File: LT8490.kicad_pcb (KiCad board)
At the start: 2 copper layers, 44 x 52 mm, 82 parts, among them Q1 TBD, Q2 TBD, Q3 TBD, Q4 TBD, Q5 BSS84, Q6 MBT2222ADW1T1, U4 LT8490EUKJPBF

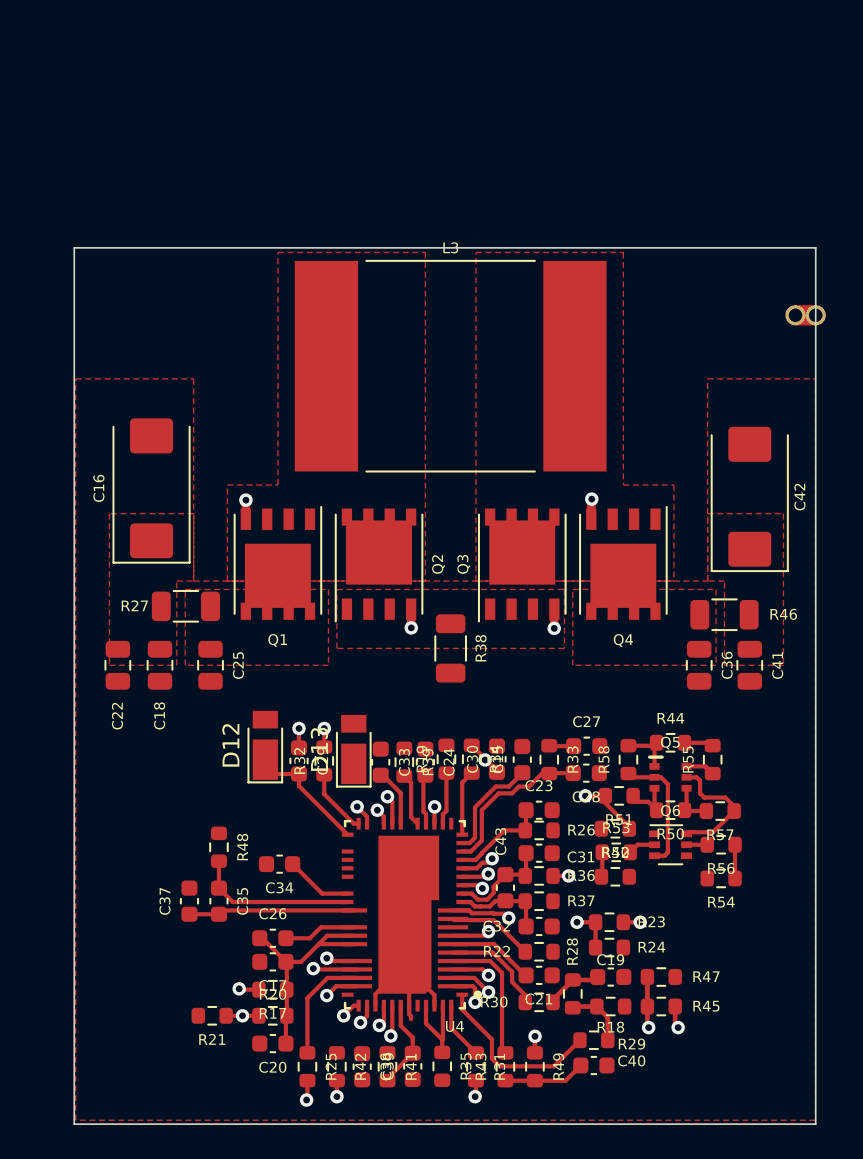
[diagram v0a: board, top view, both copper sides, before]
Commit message: routed on 6 layers. Possible to do 4?
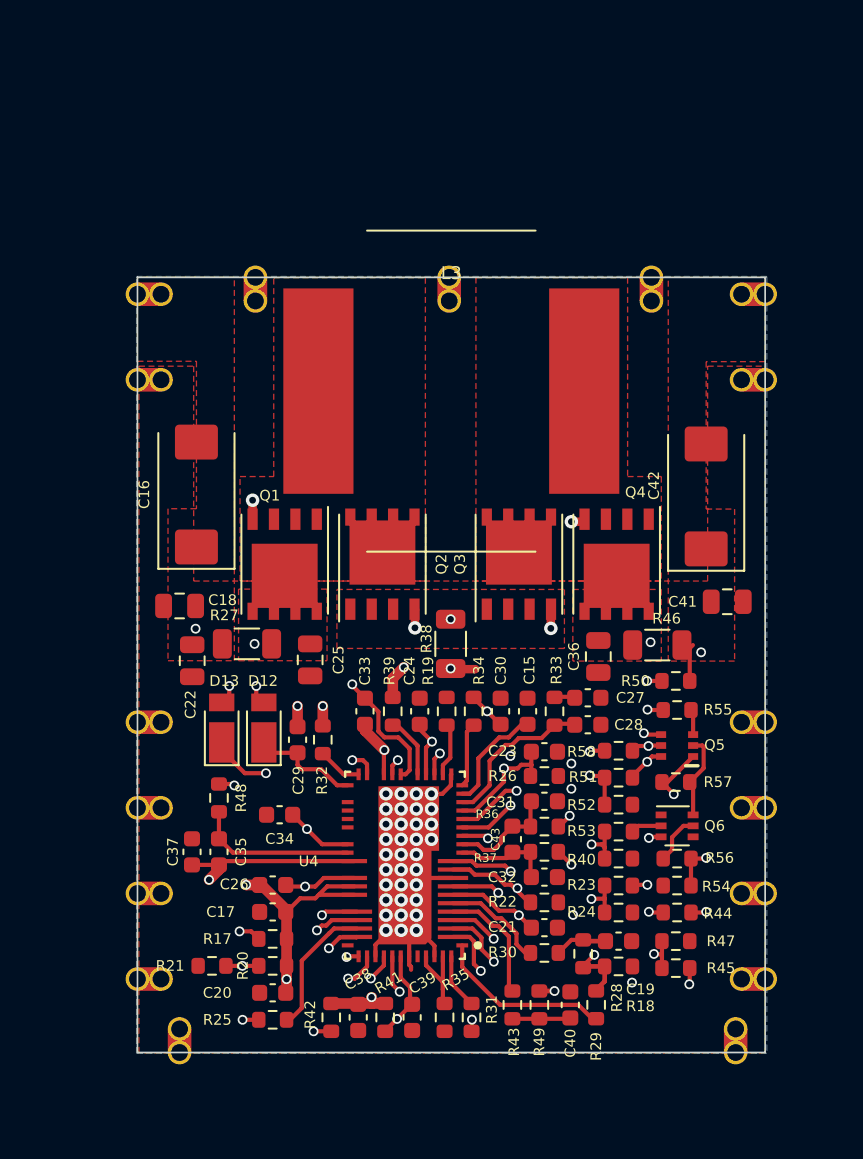
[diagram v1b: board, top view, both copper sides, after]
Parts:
- removed the REF** at (169.5, 78.0)
- added NT1: NetTie_2, NetTie:NetTie-2_SMD_Pad0.5mm, F.Cu at (148.8, 99.0)
- added REF**: castellated_05mm, custom-footprints:castellated_05mm, F.Cu at (129.2, 76.8)
- added REF**: castellated_05mm, custom-footprints:castellated_05mm, F.Cu at (166.5, 76.8)
- added REF**: castellated_05mm, custom-footprints:castellated_05mm, F.Cu at (147.8, 75.8)
- added REF**: castellated_05mm, custom-footprints:castellated_05mm, F.Cu at (136.2, 75.8)
- added REF**: castellated_05mm, custom-footprints:castellated_05mm, F.Cu at (159.8, 75.8)
- added REF**1: castellated_05mm, custom-footprints:castellated_05mm, F.Cu at (166.5, 81.8)
- added REF**10: castellated_05mm, custom-footprints:castellated_05mm, F.Cu at (129.2, 81.8)
- added REF**14: castellated_05mm, custom-footprints:castellated_05mm, F.Cu at (129.2, 102.2)
- added REF**15: castellated_05mm, custom-footprints:castellated_05mm, F.Cu at (129.2, 107.2)
- added REF**16: castellated_05mm, custom-footprints:castellated_05mm, F.Cu at (129.2, 112.3)
- added REF**17: castellated_05mm, custom-footprints:castellated_05mm, F.Cu at (129.2, 117.4)
- added REF**18: castellated_05mm, custom-footprints:castellated_05mm, F.Cu at (131.8, 121.8)
- added REF**5: castellated_05mm, custom-footprints:castellated_05mm, F.Cu at (166.5, 102.2)
- added REF**6: castellated_05mm, custom-footprints:castellated_05mm, F.Cu at (166.5, 107.2)
- added REF**7: castellated_05mm, custom-footprints:castellated_05mm, F.Cu at (166.5, 112.3)
- added REF**8: castellated_05mm, custom-footprints:castellated_05mm, F.Cu at (166.5, 117.4)
- added REF**9: castellated_05mm, custom-footprints:castellated_05mm, F.Cu at (164.8, 121.8)
- L3: footprint custom-footprints:L_SRP1770C -> custom-footprints:L_IHLP7575
- moved R44 10.1 mm to (161.3, 113.4)
- moved D13 7.94 mm to (134.2, 102.5)
- moved R50 7.68 mm to (161.2, 99.7)
- moved C36 6.01 mm to (156.6, 98.2)
- moved C25 5.92 mm to (139.5, 98.5)
- moved C22 4.42 mm to (132.5, 98.5)
- moved R46 4.37 mm to (160.1, 97.6)
- moved R27 4.26 mm to (135.8, 97.5)
- moved C41 4.00 mm to (164.2, 95.0), turned to 0 degrees
- moved C40 3.86 mm to (154.9, 118.9), turned to -90 degrees
- moved C18 3.71 mm to (131.8, 95.2), turned to 180 degrees
- moved R43 3.69 mm to (151.5, 118.9)
- moved R49 3.68 mm to (153.1, 118.9)
- moved R55 3.62 mm to (161.3, 101.4), turned to 180 degrees
- moved C23 3.49 mm to (153.4, 103.9)
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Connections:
- Q5 pad 1: V_{OUT} -> VBATT
- Q5 pad 3: Net-(Q5-Pad3) -> Net-(R55-Pad1)
- Q5 pad 4: VBATT -> V_{OUT}
- Q5 pad 5: Net-(Q5-Pad5) -> Net-(Q6-Pad3)
- Q5 pad 6: Net-(Q5-Pad6) -> Net-(R50-Pad2)
- Q6 pad 3: Net-(Q5-Pad2) -> Net-(Q6-Pad3)
- Q6 pad 6: Net-(Q5-Pad5) -> Net-(Q5-Pad2)
- R37 pad 1: GND -> Net-(NT1-Pad2)
- R38 pad 2: GND -> Net-(NT1-Pad2)
- R50 pad 2: Net-(Q5-Pad3) -> Net-(R50-Pad2)
- R51 pad 1: Net-(Q5-Pad3) -> Net-(R50-Pad2)
- R55 pad 1: Net-(Q5-Pad6) -> Net-(R55-Pad1)
- R57 pad 1: Net-(Q5-Pad5) -> Net-(Q5-Pad2)
- R58 pad 1: Net-(Q5-Pad2) -> Net-(Q6-Pad3)
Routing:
- net V_{OUT}: track 13.1 -> 66.8 mm, vias 0 -> 5
- net VBATT: track 2.67 -> 49.2 mm, vias 0 -> 3
- net VSOLAR: track 14.8 -> 55.7 mm, vias 1 -> 4
- net EXTV_{CC}: track 5.73 -> 45.9 mm, vias 0 -> 3
- net GATEV_{CC}: track 8.16 -> 46.5 mm, vias 0 -> 5
- net Net-(R17-Pad2): track 6.54 -> 41.0 mm, vias 2 -> 3
- net Net-(C23-Pad1): track 7.84 -> 39.9 mm, vias 2 -> 3
- net Net-(R49-Pad1): track 8.59 -> 40.4 mm
- net ECON: track 3.86 -> 32.5 mm, vias 1 -> 2
- net Net-(Q4-Pad4): track 2.92 -> 25.0 mm
- net SWENO: track 6.29 -> 28.2 mm, vias 2 -> 3
- net /V_{SW2}: track 0.96 -> 22.6 mm
- net Net-(NT1-Pad2): track 0.00 -> 19.6 mm, vias 0 -> 2
- net Net-(R42-Pad2): track 2.23 -> 21.5 mm
- net Net-(C33-Pad2): track 3.44 -> 22.6 mm, vias 0 -> 2
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- added copper zone on B.Cu, net GND
- added copper zone on In1.Cu, net GND
- added copper zone on In3.Cu, net GND
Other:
- board size 44 x 52 mm -> 37.2 x 46 mm
- copper layers 2 -> 6
- board text added: "Top - mixed 1 - plane 2 - sig 3 - plane 4 - sig Bot - plane"
- board text added: "Top - mixed 1 - plane 2 - sig Bot - mixed"

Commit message: evaluating layout for sensitive signals
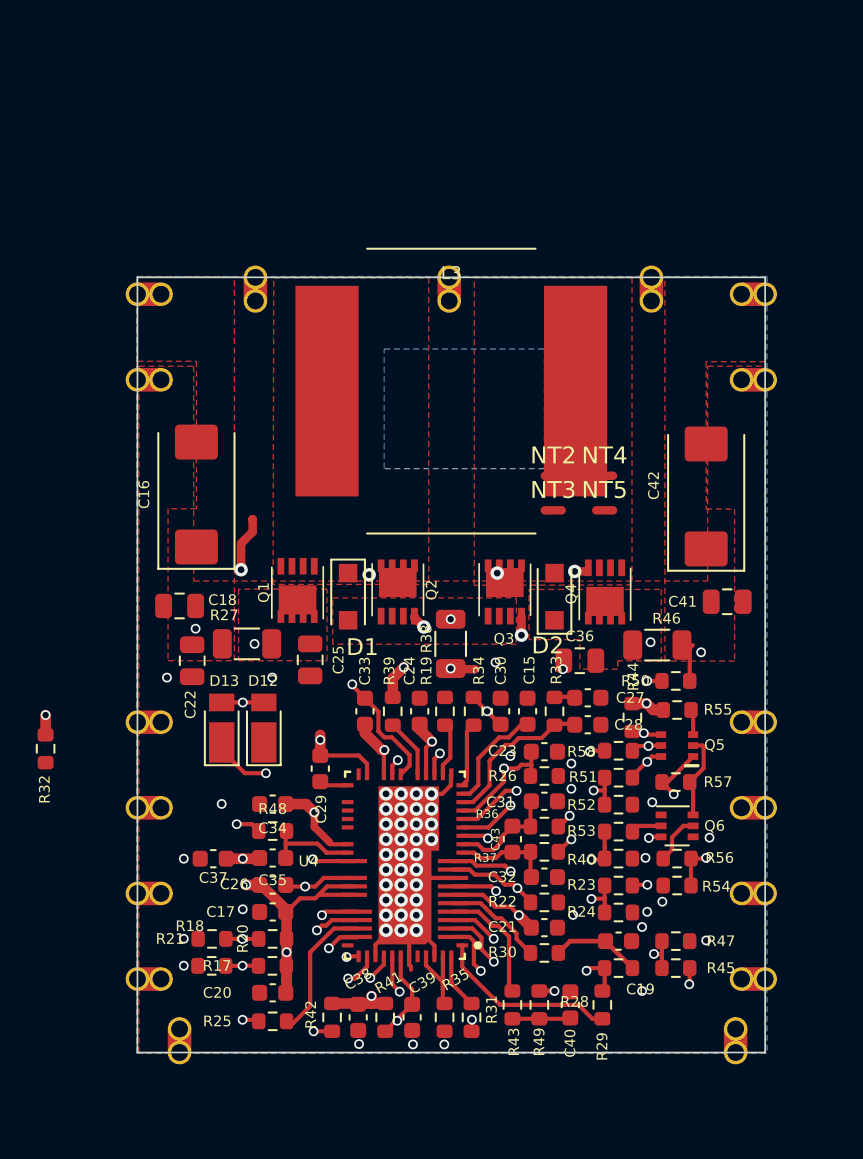
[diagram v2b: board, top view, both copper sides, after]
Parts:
- added D1: MBR1020VL, Diode_SMD:D_SOD-123F, F.Cu at (141.8, 94.7)
- added D2: MBR1020VL, Diode_SMD:D_SOD-123F, F.Cu at (154.0, 94.7)
- added NT2: NetTie_2, NetTie:NetTie-2_SMD_Pad0.5mm, F.Cu at (153.9, 87.5)
- added NT3: NetTie_2, NetTie:NetTie-2_SMD_Pad0.5mm, F.Cu at (153.9, 89.6)
- added NT4: NetTie_2, NetTie:NetTie-2_SMD_Pad0.5mm, F.Cu at (157.0, 87.5)
- added NT5: NetTie_2, NetTie:NetTie-2_SMD_Pad0.5mm, F.Cu at (157.0, 89.6)
- L3: footprint custom-footprints:L_IHLP7575 -> custom-footprints:L_SRP1770C
- Q1, Q2, Q3, Q4: value TBD -> Si7106DN; footprint Package_SO:PowerPAK_SO-8_Single -> custom-footprints:SIS862DNT1GE3
- moved R18 24.1 mm to (133.7, 116.6), turned to 180 degrees
- moved R32 16.5 mm to (123.8, 103.7)
- moved R44 11.9 mm to (158.6, 101.9), turned to 90 degrees
- moved R48 3.75 mm to (137.3, 108.6), turned to 0 degrees
- moved C35 3.21 mm to (137.3, 110.2), turned to 180 degrees
- moved R28 2.27 mm to (157.8, 116.7), turned to 180 degrees
- moved C29 2.18 mm to (140.1, 104.9)
- moved Q4 1.90 mm to (157.0, 94.5)
- moved Q1 1.84 mm to (138.8, 94.5)
- moved Q2 1.78 mm to (144.7, 94.3)
- moved Q3 1.74 mm to (151.1, 94.3)
- moved R17 1.60 mm to (137.3, 116.6)
- moved R20 1.60 mm to (137.3, 115.0)
- moved R21 1.60 mm to (133.7, 115.0)
- moved C37 1.33 mm to (133.8, 110.2), turned to 180 degrees
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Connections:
- net Net-(C29-Pad2) renamed /BOOST1
- net Net-(C33-Pad2) renamed /BOOST2
- net Net-(C35-Pad1) renamed /CSNOUT_0
- net Net-(Q1-Pad4) renamed /TG1
- net Net-(Q2-Pad4) renamed /BG1
- net Net-(Q3-Pad4) renamed /BG2
- net Net-(Q4-Pad4) renamed /TG2
- net Net-(R32-Pad1) renamed /TG1_0
- C20 pad 1: VSOLAR -> /CSPIN
- C26 pad 1: VSOLAR -> /CSPIN
- C26 pad 2: Net-(C25-Pad1) -> /CSNIN
- C35 pad 2: V_{OUT} -> /CSPOUT
- C37 pad 1: V_{OUT} -> /CSPOUT
- R48 pad 1: VBATT -> /CSNOUT
- U4 pad 42: V_{OUT} -> /CSPOUT
- U4 pad 44: Net-(C25-Pad1) -> /CSNIN
- U4 pad 45: VSOLAR -> /CSPIN
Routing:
- net Net-(C25-Pad1): track 22.5 -> 0.00 mm, vias 2 -> 0
- net /CSNIN: track 0.00 -> 21.6 mm, vias 0 -> 2
- net V_{OUT}: track 66.8 -> 50.5 mm
- net /TG1: track 16.2 -> 1.18 mm, vias 2 -> 1
- net REG_{FAULT}: track 17.9 -> 3.28 mm
- net EXTV_{CC}: track 45.9 -> 31.7 mm, vias 3 -> 2
- net REG_{STATUS}: track 12.2 -> 1.94 mm
- net /V_{SW1}: track 19.0 -> 25.2 mm, vias 2 -> 3
- net /BOOST1: track 6.45 -> 1.71 mm
- net /CSNOUT_0: track 9.58 -> 5.52 mm
- net VBATT: track 49.2 -> 52.4 mm
- net /TG1_0: track 2.63 -> 0.00 mm
- net GATEV_{CC}: track 46.5 -> 44.0 mm, vias 5 -> 4
- net Net-(C19-Pad2): track 3.05 -> 5.35 mm
- net Net-(R49-Pad1): track 40.4 -> 38.4 mm
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- added copper zone on B.Cu, net (none)
- added copper zone on In2.Cu, net GND
- added copper zone on In4.Cu, net GND

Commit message: cleaned up routing
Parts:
- removed REF**1, REF**10, REF**17, REF**18, REF**8, REF**9: castellated_05mm, custom-footprints:castellated_05mm
- added J1: Conn_01x01, custom-footprints:castellated_05mm, F.Cu at (130.7, 84.4)
- added J10: Conn_01x01, custom-footprints:castellated_05mm, F.Cu at (166.5, 117.4)
- added J2: Conn_01x01, custom-footprints:castellated_05mm, F.Cu at (130.7, 86.9)
- added J3: Conn_01x01, custom-footprints:castellated_05mm, F.Cu at (130.7, 89.5)
- added J4: Conn_01x01, custom-footprints:castellated_05mm, F.Cu at (130.7, 92.0)
- added J5: Conn_01x01, custom-footprints:castellated_05mm, F.Cu at (166.5, 84.4)
- added J6: Conn_01x01, custom-footprints:castellated_05mm, F.Cu at (166.5, 86.9)
- added J7: Conn_01x01, custom-footprints:castellated_05mm, F.Cu at (166.5, 89.5)
- added J8: Conn_01x01, custom-footprints:castellated_05mm, F.Cu at (166.5, 92.0)
- added J9: Conn_01x01, custom-footprints:castellated_05mm, F.Cu at (130.7, 117.4)
- added NT6: NetTie_2, NetTie:NetTie-2_SMD_Pad0.5mm, F.Cu at (134.1, 92.1)
- added NT7: NetTie_2, NetTie:NetTie-2_SMD_Pad0.5mm, F.Cu at (161.6, 92.1)
- added R1: 10, Resistor_SMD:R_0603_1608Metric, F.Cu at (134.8, 107.6)
- added REF**: Fiducial_0.75mm_Mask1.5mm, Fiducial:Fiducial_0.75mm_Mask1.5mm, F.Cu at (160.9, 120.0)
- added REF**: Fiducial_0.75mm_Mask1.5mm, Fiducial:Fiducial_0.75mm_Mask1.5mm, F.Cu at (164.3, 77.2)
- added REF**: Fiducial_0.75mm_Mask1.5mm, Fiducial:Fiducial_0.75mm_Mask1.5mm, F.Cu at (130.8, 77.2)
- added Ref**: Val**, custom-footprints:holliday, F.Cu at (134.9, 120.8)
- added kibuzzard-623CC1D5: G***, kibuzzard-623CC1D5, F.Cu at (130.3, 81.8)
- added kibuzzard-623CC1D5: G***, kibuzzard-623CC1D5, F.Cu at (165.5, 81.8)
- added kibuzzard-623CC1F4: G***, kibuzzard-623CC1F4, F.Cu at (130.3, 95.3)
- added kibuzzard-623CC23C: G***, kibuzzard-623CC23C, F.Cu at (165.5, 94.9)
- added kibuzzard-623CC3F2: G***, kibuzzard-623CC3F2, F.Cu at (131.2, 119.2)
- added kibuzzard-623CC40F: G***, kibuzzard-623CC40F, F.Cu at (164.2, 119.2)
- D12, D13: value DFLS130L -> CMMR1U-02 TR; footprint Diode_SMD:D_PowerDI-123 -> Diode_SMD:D_SOD-123F
- moved NT2 21.9 mm to (134.5, 97.6), turned to 90 degrees
- moved NT3 18.6 mm to (137.2, 97.6), turned to 90 degrees
- moved R32 14.8 mm to (138.6, 104.1)
- moved NT4 10.2 mm to (158.6, 97.6), turned to 90 degrees
- moved NT5 9.24 mm to (161.6, 97.6), turned to 90 degrees
- moved C20 6.84 mm to (135.6, 111.6)
- moved D13 4.52 mm to (138.3, 100.6), turned to 180 degrees
- moved REF** 2.54 mm to (129.2, 79.3)
- moved REF** 2.54 mm to (166.5, 79.3)
- moved C37 1.87 mm to (135.6, 110.0)
- moved C16 1.76 mm to (134.5, 88.8)
- moved C42 1.75 mm to (161.2, 88.8)
- moved R25 1.68 mm to (137.1, 118.2)
- moved C26 1.44 mm to (138.7, 111.6)
- moved C35 1.44 mm to (138.7, 110.0)
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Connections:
- net Net-(Q5-Pad6) renamed /FBOUT_0
- net Net-(R39-Pad2) renamed /BG2_
- C17 pad 1: VSOLAR -> /FBIN
- C26 pad 2: /CSNIN -> /CSNIN_0
- NT5 pad 1: (no net) -> /CSNOUT
- Q5 pad 1: VBATT -> /FBOUT
- R17 pad 1: VSOLAR -> /FBIN
- R20 pad 1: VSOLAR -> /FBIN
- R23 pad 1: VSOLAR -> /FBIN
- R37 pad 1: Net-(NT1-Pad2) -> Net-(C32-Pad2)
- R37 pad 2: Net-(C32-Pad2) -> Net-(NT1-Pad2)
- R38 pad 2: Net-(NT1-Pad2) -> GND
- R50 pad 1: VBATT -> /FBOUT
- R57 pad 2: VBATT -> /FBOUT
- U4 pad 44: /CSNIN -> /CSNIN_0
- U4 pad 46: VSOLAR -> /FBIN
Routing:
- net /FBIN: track 0.00 -> 59.8 mm, vias 0 -> 4
- net VSOLAR: track 55.8 -> 0.00 mm, vias 4 -> 3
- net VBATT: track 52.4 -> 0.00 mm
- net /CSPOUT: track 0.00 -> 45.5 mm, vias 0 -> 2
- net /CSNOUT: track 0.00 -> 41.7 mm, vias 0 -> 2
- net V_{OUT}: track 50.5 -> 12.3 mm, vias 5 -> 3
- net /CSPIN: track 0.00 -> 24.7 mm, vias 0 -> 2
- net /CSNIN: track 21.6 -> 0.00 mm, vias 2 -> 1
- net /FBOUT: track 0.00 -> 19.6 mm, vias 0 -> 3
- net GND: track 8.11 -> 26.2 mm, vias 57 -> 70
- net REG_{FAULT}: track 3.28 -> 21.4 mm, vias 1 -> 2
- net Net-(NT1-Pad2): track 18.1 -> 0.00 mm, vias 2 -> 0
- net REG_{STATUS}: track 1.94 -> 17.5 mm, vias 1 -> 2
- net /BOOST2: track 22.2 -> 8.50 mm, vias 2 -> 0
- net /CSNIN_0: track 0.00 -> 12.4 mm, vias 0 -> 2
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- added copper zone on In4.Cu, net VBATT
- added copper zone on B.Cu, net VSOLAR
- added copper zone on In4.Cu, net VSOLAR
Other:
- board text added: "C_{C1}"
- board text added: "C_{C2}"
- board text added: "R_{DACI1}"
- board text added: "R_{DACI2}"
- board text added: "V_{FBIN}"
- board text added: "V_{FBOUT}"
- board text added: "V_{INR}"
- board text added: "~{SHDN}"
- board text removed: "Top - mixed 1 - plane 2 - sig 3 - plane 4 - sig Bot - plane"
- board text removed: "Top - mixed 1 - plane 2 - sig Bot - mixed"
